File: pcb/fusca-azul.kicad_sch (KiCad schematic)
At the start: 6 parts, among them J1 L298N Logic Jumpers, J2 HC-SR04, U1 ESP32-DEVKIT-V1

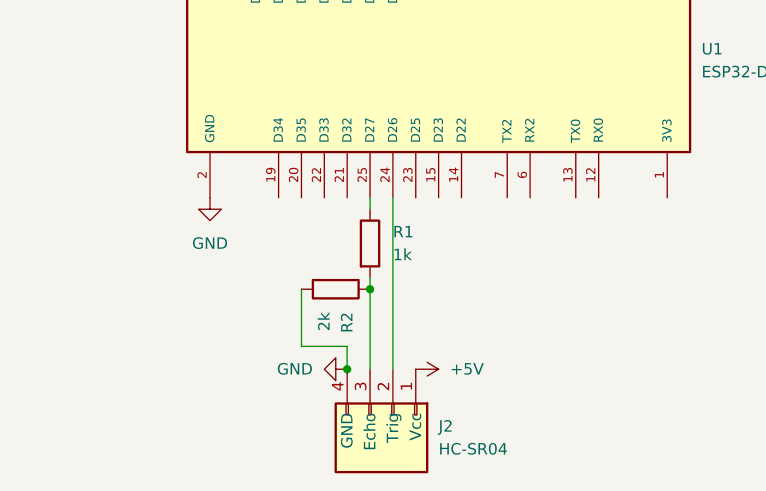
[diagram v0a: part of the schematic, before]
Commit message: fix: corrige posicionamento errado dos resistores
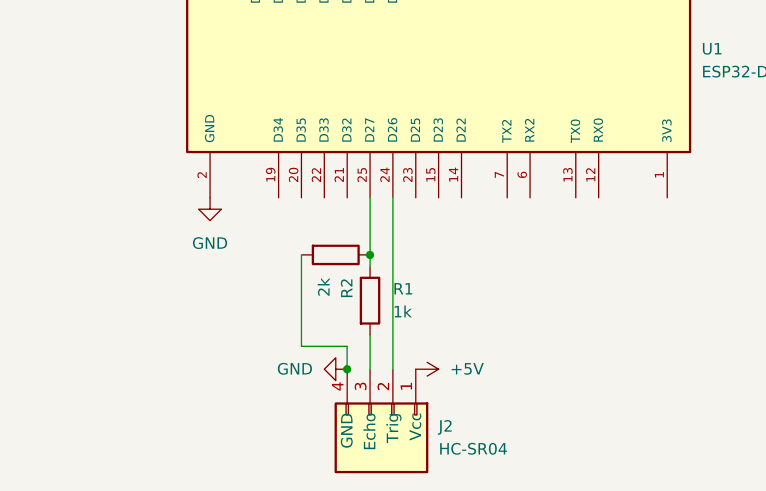
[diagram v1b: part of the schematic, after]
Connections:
- net at J2.3 (Echo), R1.2: no longer R2.1
- net at R1.1, U1.25 (D27): now also R2.1
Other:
- moved on the sheet: R1, R2
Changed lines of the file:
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@@
 	(paper "A4")
 	(junction
-		(at 114.3 99.06)
+		(at 114.3 95.25)
 		(diameter 0)
 		(color 0 0 0 0)
@@
 	(wire
 		(pts
-			(xy 114.3 97.79) (xy 114.3 99.06)
+			(xy 106.68 45.72) (xy 106.68 58.42)
 		)
 		(stroke
@@
 	(wire
 		(pts
-			(xy 106.68 45.72) (xy 106.68 58.42)
+			(xy 114.3 88.9) (xy 114.3 95.25)
 		)
 		(stroke
@@
 	(wire
 		(pts
-			(xy 114.3 88.9) (xy 114.3 90.17)
+			(xy 111.76 45.72) (xy 111.76 58.42)
 		)
 		(stroke
@@
 	(wire
 		(pts
-			(xy 111.76 45.72) (xy 111.76 58.42)
+			(xy 116.84 88.9) (xy 116.84 107.95)
 		)
 		(stroke
@@
 	(wire
 		(pts
-			(xy 116.84 88.9) (xy 116.84 107.95)
+			(xy 109.22 45.72) (xy 109.22 58.42)
 		)
 		(stroke
@@
 	(wire
 		(pts
-			(xy 109.22 45.72) (xy 109.22 58.42)
+			(xy 114.3 104.14) (xy 114.3 107.95)
 		)
 		(stroke
@@
 	(wire
 		(pts
-			(xy 114.3 99.06) (xy 114.3 107.95)
+			(xy 114.3 45.72) (xy 114.3 58.42)
 		)
 		(stroke
@@
 	(wire
 		(pts
-			(xy 114.3 45.72) (xy 114.3 58.42)
+			(xy 114.3 95.25) (xy 114.3 96.52)
 		)
 		(stroke
@@
 	(wire
 		(pts
-			(xy 106.68 99.06) (xy 106.68 105.41)
+			(xy 106.68 95.25) (xy 106.68 105.41)
 		)
 		(stroke
@@
 	(symbol
 		(lib_id "Device:R")
-		(at 110.49 99.06 270)
+		(at 110.49 95.25 270)
 		(unit 1)
 		(body_style 1)
@@
 		(dnp no)
 		(property "Reference" "R2"
-			(at 111.7601 101.6 0)
+			(at 111.7601 97.79 0)
 			(show_name no)
 			(do_not_autoplace no)
@@
 		)
 		(property "Value" "2k"
-			(at 109.2201 101.6 0)
+			(at 109.2201 97.79 0)
 			(show_name no)
 			(do_not_autoplace no)
@@
 		)
 		(property "Footprint" ""
-			(at 110.49 97.282 90)
+			(at 110.49 93.472 90)
 			(hide yes)
 			(show_name no)
@@
 		)
 		(property "Datasheet" ""
-			(at 110.49 99.06 0)
+			(at 110.49 95.25 0)
 			(hide yes)
 			(show_name no)
@@
 		)
 		(property "Description" "Resistor"
-			(at 110.49 99.06 0)
+			(at 110.49 95.25 0)
 			(hide yes)
 			(show_name no)
@@
 	(symbol
 		(lib_id "Device:R")
-		(at 114.3 93.98 0)
+		(at 114.3 100.33 0)
 		(unit 1)
 		(body_style 1)
@@
 		(fields_autoplaced yes)
 		(property "Reference" "R1"
-			(at 116.84 92.7099 0)
+			(at 116.84 99.0599 0)
 			(show_name no)
 			(do_not_autoplace no)
@@
 		)
 		(property "Value" "1k"
-			(at 116.84 95.2499 0)
+			(at 116.84 101.5999 0)
 			(show_name no)
 			(do_not_autoplace no)
@@
 		)
 		(property "Footprint" ""
-			(at 112.522 93.98 90)
+			(at 112.522 100.33 90)
 			(hide yes)
 			(show_name no)
@@
 		)
 		(property "Datasheet" ""
-			(at 114.3 93.98 0)
+			(at 114.3 100.33 0)
 			(hide yes)
 			(show_name no)
@@
 		)
 		(property "Description" "Resistor"
-			(at 114.3 93.98 0)
-			(hide yes)
-			(show_name no)
+			(at 114.3 100.33 0)
+			(hide yes)
+			(show_name no)

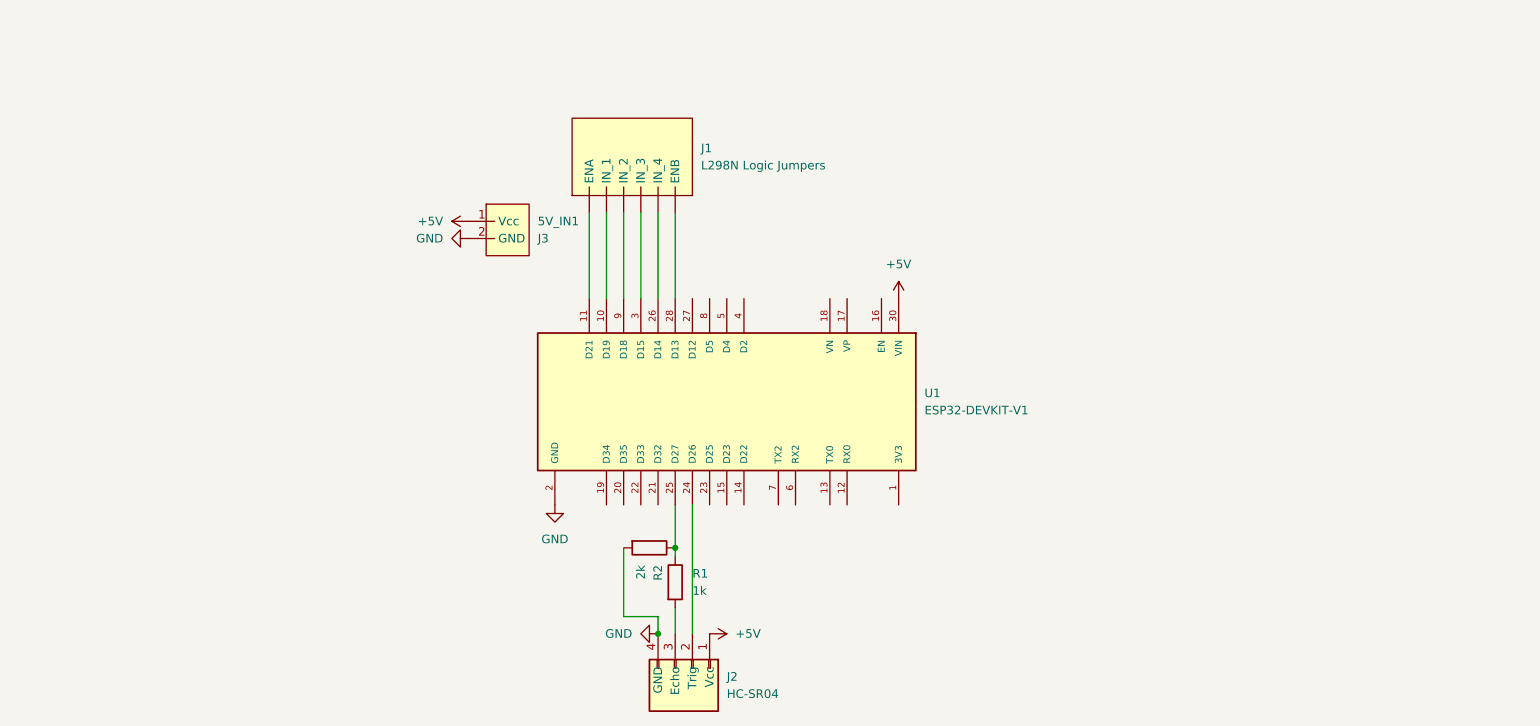
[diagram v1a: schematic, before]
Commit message: feat: adiciona schematic para 3 sensores + separa schematics
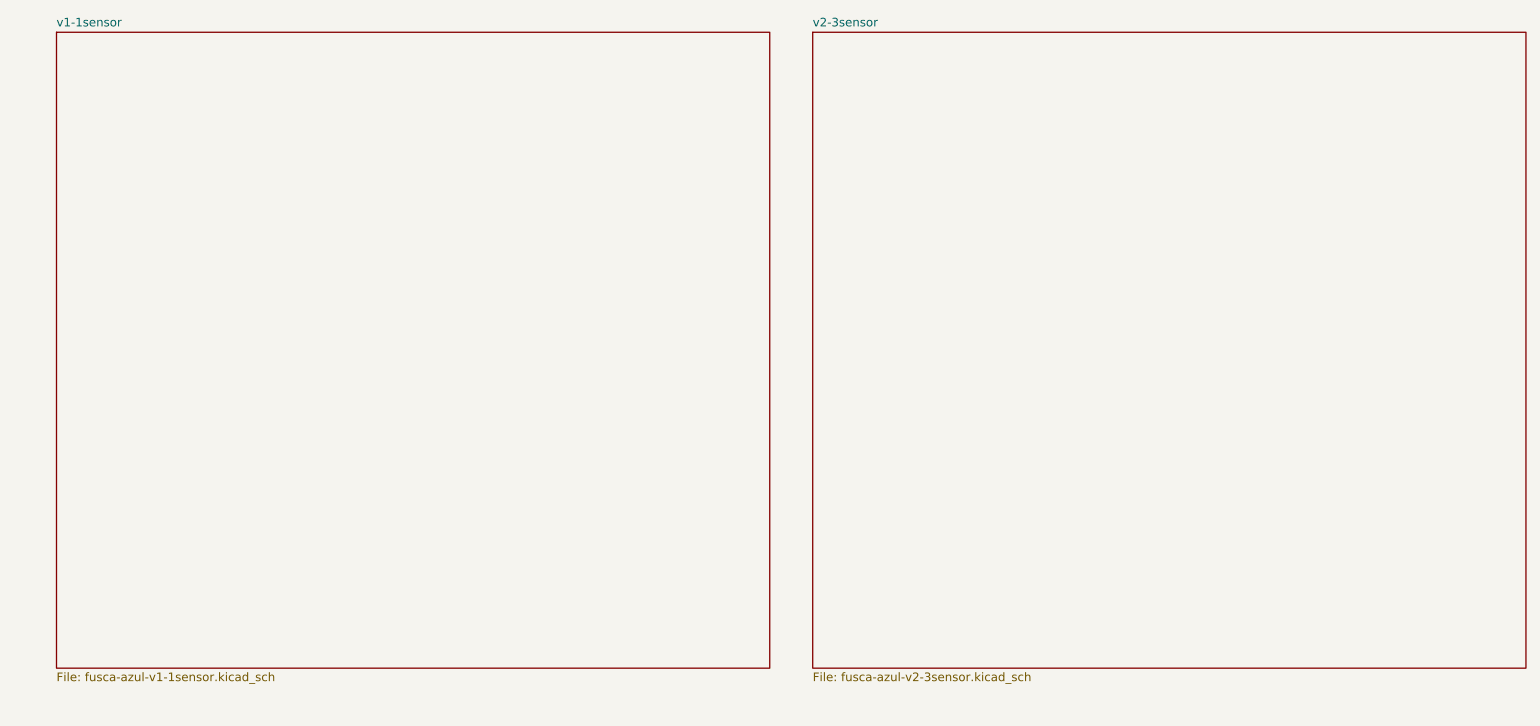
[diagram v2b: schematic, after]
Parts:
- removed 5V_IN1: J3, symbol fusca-azul:5V_IN
- removed J1: L298N Logic Jumpers, symbol fusca-azul:L298N - Logic Jumpers
- removed J2: HC-SR04, symbol fusca-azul:HC-SR04
- removed R1: 1k, symbol Device:R
- removed R2: 2k, symbol Device:R
- removed U1: ESP32-DEVKIT-V1, ESP32-DEVKIT-V1:MODULE_ESP32_DEVKIT_V1, symbol ESP32-DEVKIT-V1:ESP32-DEVKIT-V1
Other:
- added sheet v1-1sensor (fusca-azul-v1-1sensor.kicad_sch)
- added sheet v2-3sensor (fusca-azul-v2-3sensor.kicad_sch)

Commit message: feat: atualiza a pcb, mas falta corrigir tamanho e organização
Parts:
- added 5V_IN1: J3, TerminalBlock_Phoenix:TerminalBlock_Phoenix_MKDS-1,5-2-5.08_1x02_P5.08mm_Horizontal, symbol fusca-azul:5V_IN
- added J3, J5, J6: HC-SR04, Connector_PinSocket_2.54mm:PinSocket_1x04_P2.54mm_Vertical, symbol fusca-azul:HC-SR04
- added J4: L298N Logic Jumpers, Connector_PinSocket_2.54mm:PinSocket_1x06_P2.54mm_Vertical, symbol fusca-azul:L298N - Logic Jumpers
- added R3, R5, R7: 2k, Resistor_THT:R_Axial_DIN0207_L6.3mm_D2.5mm_P2.54mm_Vertical, symbol Device:R
- added R4, R6, R8: 1k, Resistor_THT:R_Axial_DIN0207_L6.3mm_D2.5mm_P2.54mm_Vertical, symbol Device:R
- added U2: ESP32 - HW-394, fusca-azul:ESP32-HW-394, symbol fusca-azul:ESP32_-_HW_394
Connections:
- new net: R3.1, R4.1, U2.29 (D22)
- new net: J5.2 (Trig), U2.30 (D23)
- new net: J5.3 (Echo), R6.2
- new net: J4.1 (ENA), U2.3 (D13)
- new net: J4.2 (IN_1), U2.5 (D14)
- new net: J4.3 (IN_2), U2.6 (D27)
- new net: J4.4 (IN_3), U2.7 (D26)
- new net: J4.5 (IN_4), U2.8 (D25)
- new net: J4.6 (ENB), U2.9 (D33)
- new net: R5.2, R6.1, U2.12 (D34)
- new net: J6.2 (Trig), U2.10 (D32)
- new net: J6.3 (Echo), R8.2
- new net: R7.1, R8.1, U2.11 (D35)
- new net: J3.3 (Echo), R4.2
- new net: J3.2 (Trig), U2.26 (D21)
- new net +5V: 5V_IN1.2 (Vcc), J3.1 (Vcc), J5.1 (Vcc), J6.1 (Vcc), U2.1 (VIN)
- new net GND: 5V_IN1.1 (GND), J3.4 (GND), J5.4 (GND), J6.4 (GND), R3.2, R5.1, R7.2, U2.17 (GND), U2.2 (GND)
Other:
- removed sheet v1-1sensor
- removed sheet v2-3sensor

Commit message: feat: finaliza pcb
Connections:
- net GND: now also R5.2; no longer R5.1
- net at R3.1, R4.1: now also U2.21 (RX2); no longer U2.29 (D22)
- net at J5.2 (Trig): now also U2.9 (D33); no longer U2.30 (D23)
- net at J4.1 (ENA): now also U2.22 (TX2); no longer U2.3 (D13)
- net at J4.2 (IN_1): now also U2.24 (D18); no longer U2.5 (D14)
- net at J4.3 (IN_2): now also U2.25 (D19); no longer U2.6 (D27)
- net at J4.4 (IN_3): now also U2.26 (D21); no longer U2.7 (D26)
- net at U2.8 (D25): now also R5.1, R6.1; no longer J4.5 (IN_4)
- net at J4.6 (ENB): now also U2.30 (D23); no longer U2.9 (D33)
- net at J6.2 (Trig): now also U2.18 (D15); no longer U2.10 (D32)
- net at J6.3 (Echo): now also R4.2; no longer R8.2
- net at J3.3 (Echo): now also R8.1; no longer R4.2
- net at J3.2 (Trig): no longer U2.26 (D21)
- new net: J4.5 (IN_4), U2.29 (D22)
- new net: R7.1, R8.2
- now unconnected: U2.11 (D35), U2.12 (D34)
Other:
- moved on the sheet: 5V_IN1, J3, J4, J5, U2

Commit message: fix: corrige ligacao na placa
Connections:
- net at R7.1, R8.2: now also U2.7 (D26)
- net at J3.2 (Trig): now also U2.6 (D27)
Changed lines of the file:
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@@
 	(paper "A4")
 	(junction
+		(at 86.36 57.15)
+		(diameter 0)
+		(color 0 0 0 0)
+	)
+	(junction
 		(at 104.14 64.77)
 		(diameter 0)
@@
 	(wire
 		(pts
+			(xy 100.33 77.47) (xy 86.36 77.47)
+		)
+		(stroke
+			(width 0)
+			(type default)
+		)
+	)
+	(wire
+		(pts
 			(xy 74.93 97.79) (xy 67.31 97.79)
 		)
@@
 	(wire
 		(pts
+			(xy 88.9 74.93) (xy 100.33 74.93)
+		)
+		(stroke
+			(width 0)
+			(type default)
+		)
+	)
+	(wire
+		(pts
 			(xy 66.04 90.17) (xy 68.58 90.17)
 		)
@@
 	(wire
 		(pts
+			(xy 88.9 46.99) (xy 88.9 74.93)
+		)
+		(stroke
+			(width 0)
+			(type default)
+		)
+	)
+	(wire
+		(pts
 			(xy 104.14 71.12) (xy 104.14 64.77)
 		)
@@
 		)
 		(stroke
+			(width 0)
+			(type default)
+		)
+	)
+	(wire
+		(pts
+			(xy 86.36 77.47) (xy 86.36 57.15)
+		)
+		(stroke

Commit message: finaliza pcb
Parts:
- removed J6: HC-SR04, Connector_PinSocket_2.54mm:PinSocket_1x04_P2.54mm_Vertical, symbol fusca-azul:HC-SR04
- removed R3: 2k, Resistor_THT:R_Axial_DIN0207_L6.3mm_D2.5mm_P2.54mm_Vertical, symbol Device:R
- removed R4: 1k, Resistor_THT:R_Axial_DIN0207_L6.3mm_D2.5mm_P2.54mm_Vertical, symbol Device:R
- R5, R6, R7, R8: footprint Resistor_THT:R_Axial_DIN0207_L6.3mm_D2.5mm_P2.54mm_Vertical -> Resistor_THT:R_Axial_DIN0207_L6.3mm_D2.5mm_P5.08mm_Vertical
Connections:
- net GND: now also R7.1; no longer R7.2
- net at J5.3 (Echo): now also R6.1; no longer R6.2
- net at U2.9 (D33): now also J3.2 (Trig); no longer J5.2 (Trig)
- net at J4.1 (ENA): now also U2.30 (D23); no longer U2.22 (TX2)
- net at J4.2 (IN_1): now also U2.29 (D22); no longer U2.24 (D18)
- net at J4.3 (IN_2): now also U2.26 (D21); no longer U2.25 (D19)
- net at J4.4 (IN_3): now also U2.25 (D19); no longer U2.26 (D21)
- net at J4.5 (IN_4): now also U2.24 (D18); no longer U2.29 (D22)
- net at J4.6 (ENB): now also U2.20 (D4); no longer U2.30 (D23)
- net at R8.2, U2.7 (D26): now also R7.2; no longer R7.1
- net at U2.6 (D27): now also J5.2 (Trig); no longer J3.2 (Trig)
- net at U2.5 (D14): now also R5.1, R6.2
- now unconnected: U2.8 (D25)
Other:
- moved on the sheet: 5V_IN1, J4, R5, R6, R7, R8
